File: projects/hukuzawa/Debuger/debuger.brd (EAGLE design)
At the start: 100 x 72 mm, 39 parts, among them IC1 PIC16F886, J1 3X1A

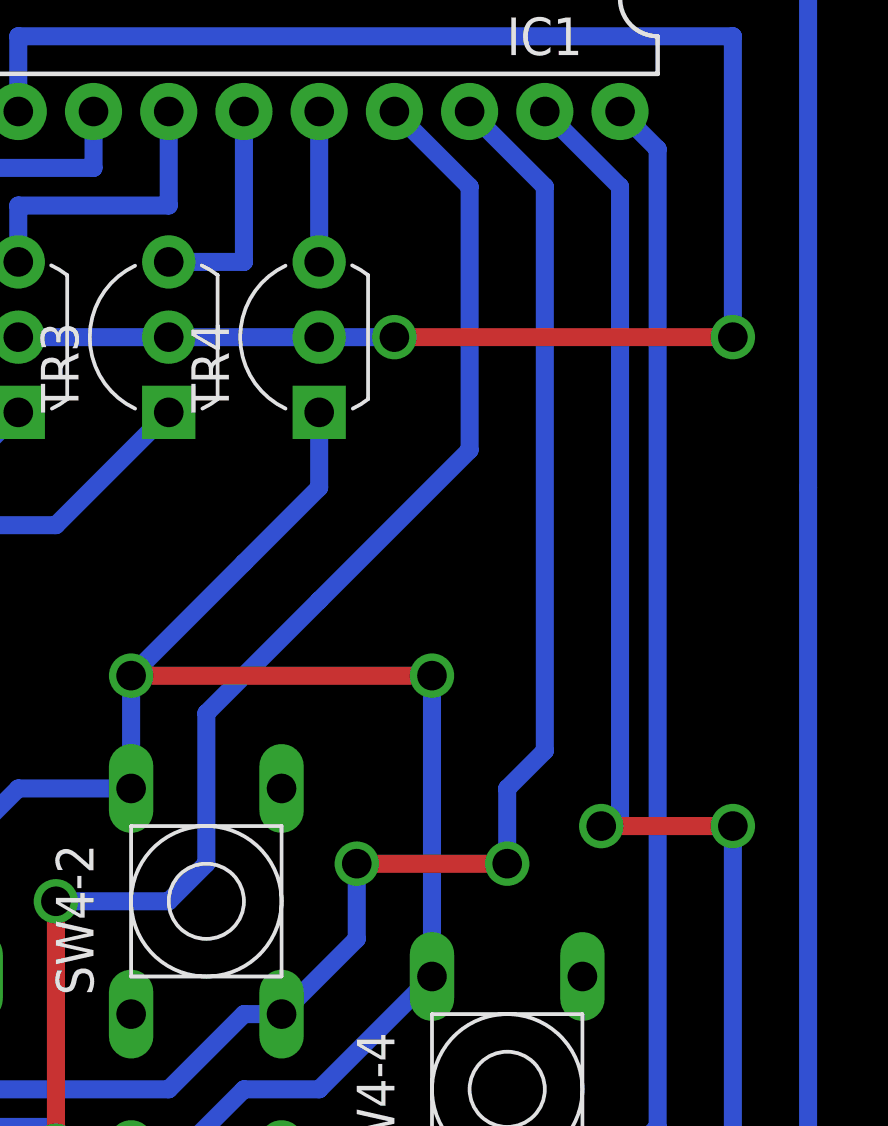
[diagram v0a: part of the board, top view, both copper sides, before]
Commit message: デバッガ基板微修正
配線を修正、ジャンパを1個削減
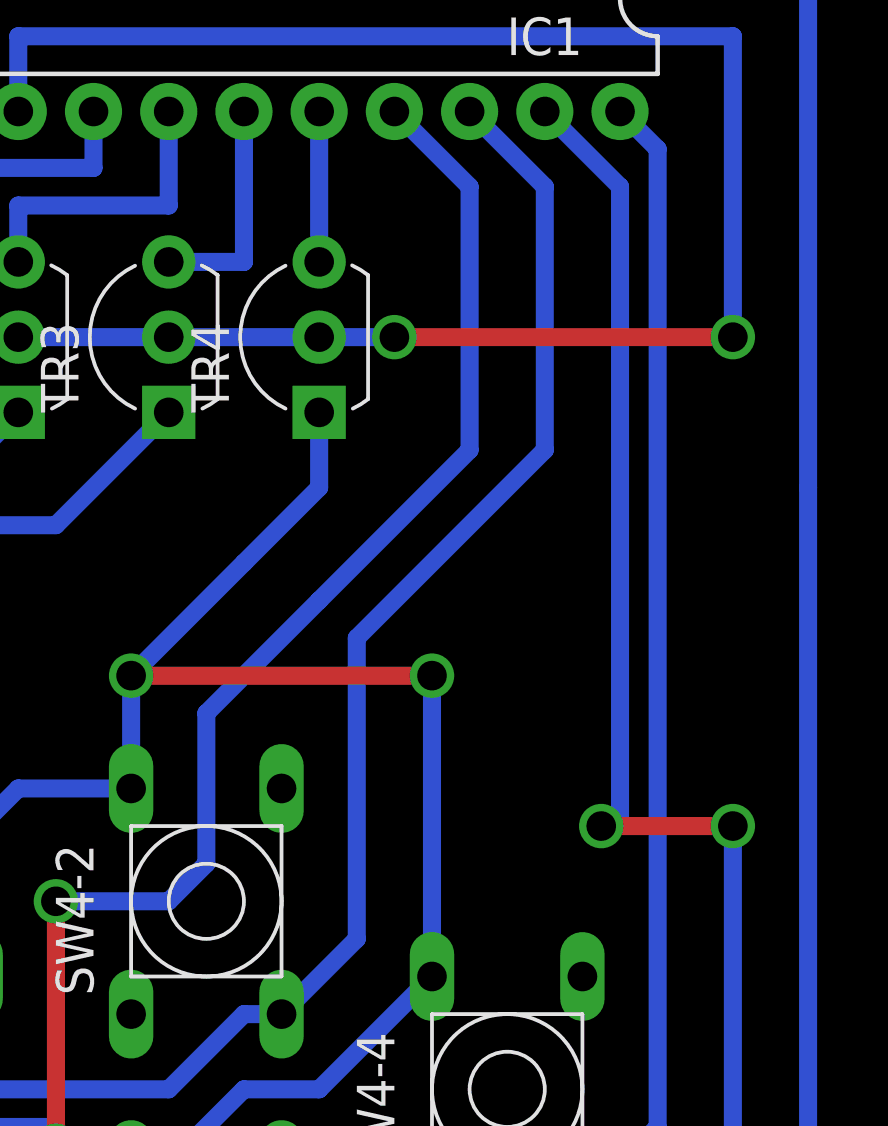
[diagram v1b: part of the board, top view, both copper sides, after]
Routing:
- net BR2: track 133.0 -> 130.0 mm, vias 6 -> 4
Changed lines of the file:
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@@
 <wire x1="72.39" y1="17.78" x2="74.93" y2="20.32" width="0.6096" layer="16"/>
 <wire x1="74.93" y1="20.32" x2="76.2" y2="20.32" width="0.6096" layer="16"/>
-<via x="78.74" y="25.4" extent="1-16" drill="1"/>
-<wire x1="78.74" y1="25.4" x2="83.82" y2="25.4" width="0.6096" layer="1"/>
-<via x="83.82" y="25.4" extent="1-16" drill="1"/>
-<wire x1="83.82" y1="25.4" x2="83.82" y2="27.94" width="0.6096" layer="16"/>
-<wire x1="83.82" y1="27.94" x2="85.09" y2="29.21" width="0.6096" layer="16"/>
-<wire x1="85.09" y1="29.21" x2="85.09" y2="48.26" width="0.6096" layer="16"/>
 <wire x1="85.09" y1="48.26" x2="82.55" y2="50.8" width="0.6096" layer="16"/>
 <wire x1="25.4" y1="36.83" x2="22.86" y2="39.37" width="0.6096" layer="16"/>
@@
 <wire x1="26.67" y1="35.56" x2="30.48" y2="35.56" width="0.6096" layer="16"/>
 <wire x1="76.2" y1="20.32" x2="78.74" y2="22.86" width="0.6096" layer="16"/>
-<wire x1="78.74" y1="22.86" x2="78.74" y2="25.4" width="0.6096" layer="16"/>
+<wire x1="78.74" y1="22.86" x2="78.74" y2="33.02" width="0.6096" layer="16"/>
+<wire x1="78.74" y1="33.02" x2="85.09" y2="39.37" width="0.6096" layer="16"/>
+<wire x1="85.09" y1="39.37" x2="85.09" y2="48.26" width="0.6096" layer="16"/>
 </signal>
 <signal name="BR3">
